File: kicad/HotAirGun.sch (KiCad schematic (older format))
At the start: 0 parts

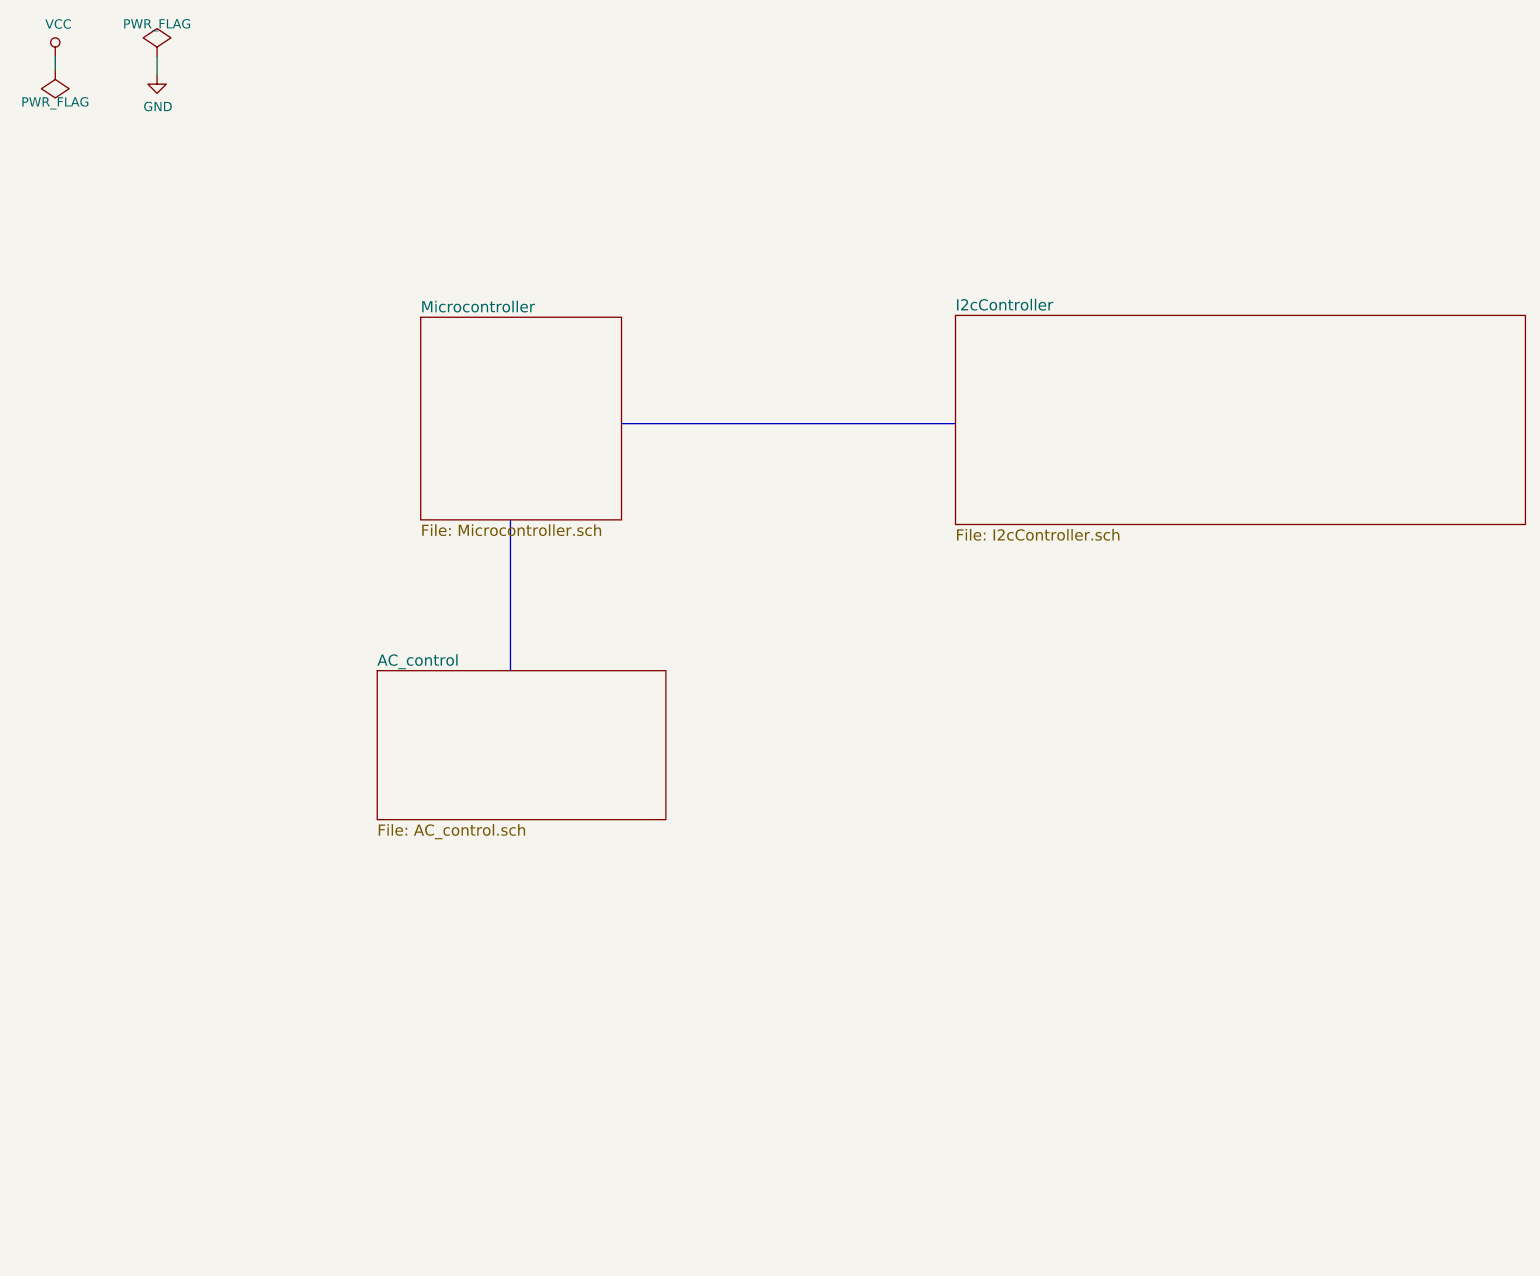
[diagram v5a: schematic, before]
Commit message: Add Gun image to general schematic
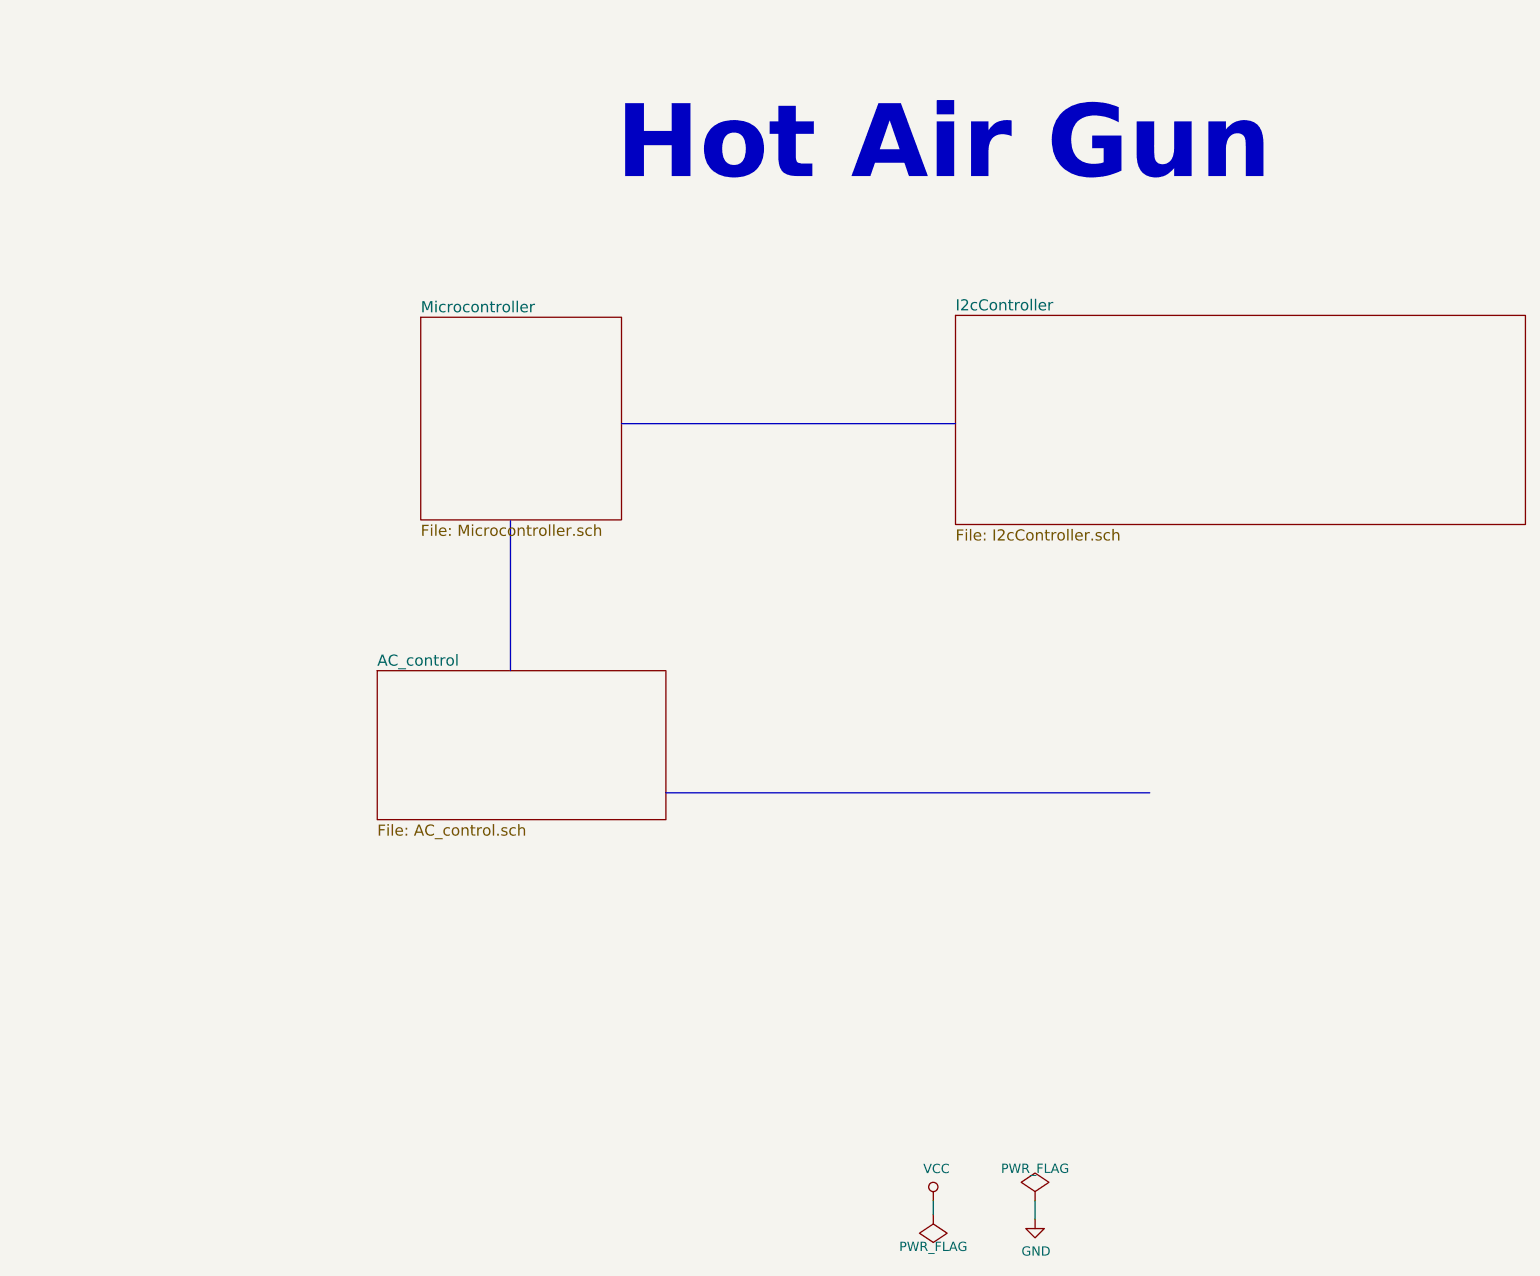
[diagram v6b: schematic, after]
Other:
- note added: "Hot Air Gun"
